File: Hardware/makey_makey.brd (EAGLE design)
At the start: 94 x 48.3 mm, 73 parts, among them U1 ATMEGA32U4TQFP, X1 USBSMD, Y1 16MHz

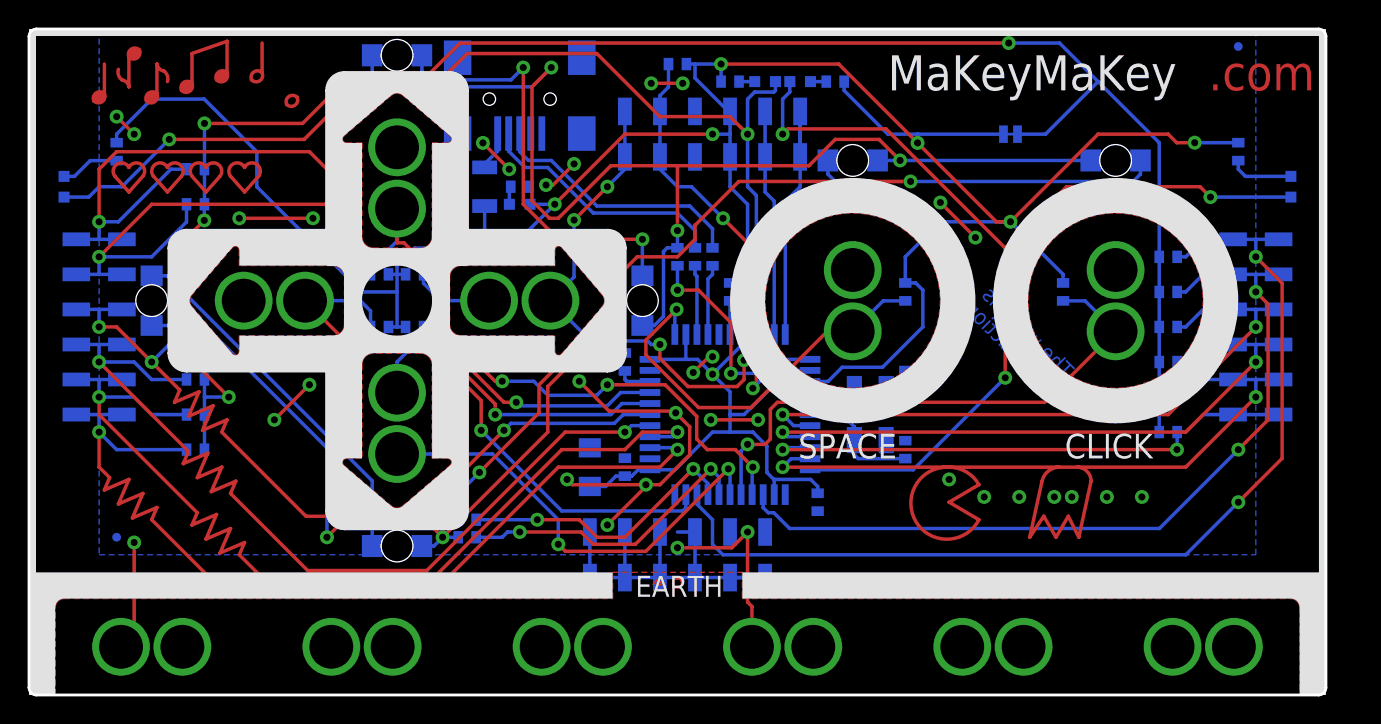
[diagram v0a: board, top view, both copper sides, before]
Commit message: QC Revision
1.) Switch 0402 to 0603 footprints
2.) Updated to wide PTC footprint
3.) Added more bstop over lead banks on 32u4 IC for better AOI.
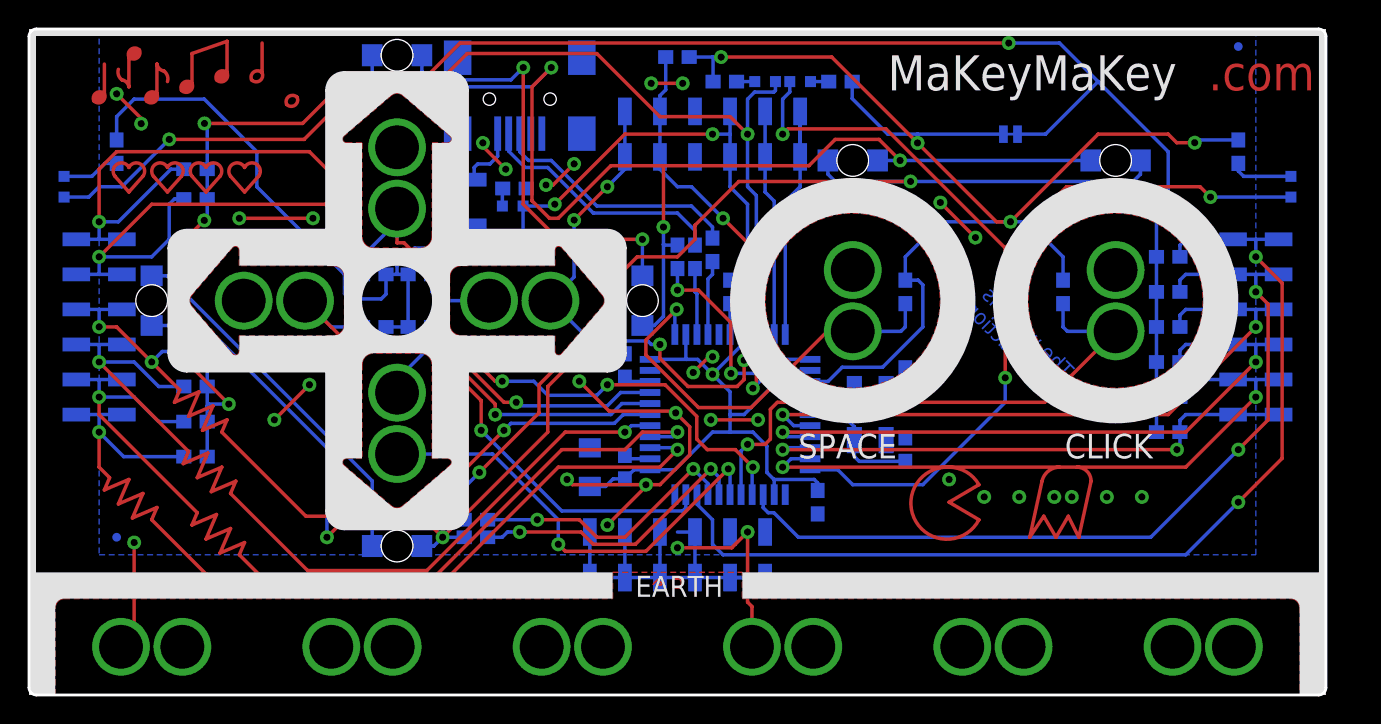
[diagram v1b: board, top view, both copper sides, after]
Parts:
- C1, C2, C3, C4, C5, C6, C8: device SparkFun:0402-CAP -> SparkFun:0603-CAP
- F1: device SparkFun-PowerIC:PTC-1206 -> SparkFun-PowerIC:PTC-1206-WIDE
- R1, R10, R11, R12, R13, R14, R15, R2, R23, R24, R25, R26, R27, R28, R29, R3, R4, R5, R6, R7, R8, R9: device SparkFun:0402-RES -> SparkFun:0603-RES
- R16, R17, R18, R19, R20, R21, R22: device SparkFun-Passives:0402-RES -> SparkFun-Passives:0603-RES
- moved F1 1.37 mm to (32.3, 35.7)
- moved C8 0.85 mm to (30.1, 36.1)
- moved R20 0.63 mm to (32.4, 11.4)
- moved R21 0.63 mm to (32.4, 12.7)
- moved LED7 0.52 mm to (35.1, 35.4)
- moved R2 0.51 mm to (49.5, 32.3)
- moved R3 0.51 mm to (47.0, 46.2)
- moved R4 0.51 mm to (12.1, 17.3)
- moved R5 0.51 mm to (12.1, 19.8)
- moved R6 0.51 mm to (12.1, 22.4)
- moved R7 0.51 mm to (12.1, 24.9)
- moved R23 0.40 mm to (35.2, 36.7)
- moved R16 0.38 mm to (58.8, 44.5)
- moved R19 0.38 mm to (50.4, 44.5)
- moved R24 0.38 mm to (25.0, 30.5)
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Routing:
- net VCC: track 233.0 -> 229.7 mm
- net GND: track 104.3 -> 107.2 mm
- net PD5: track 73.0 -> 75.0 mm
- net N$5: track 2.84 -> 4.56 mm
- net D13: track 42.4 -> 41.2 mm
- net PULL-UP: track 134.5 -> 135.7 mm
- net D7: track 29.7 -> 30.6 mm
- net D6: track 39.9 -> 40.8 mm
- net D9: track 21.9 -> 21.1 mm
- net D10: track 20.6 -> 19.8 mm
- net D4: track 60.2 -> 61.0 mm
- net A4: track 66.0 -> 66.7 mm
- net N$8: track 19.0 -> 18.3 mm

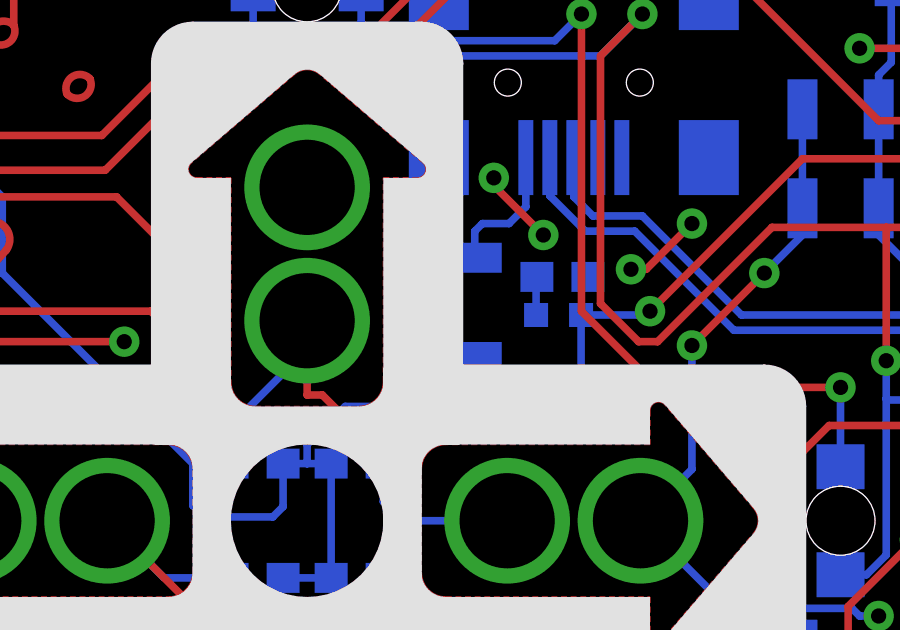
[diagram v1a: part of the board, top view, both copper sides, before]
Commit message: Swapped positions of PTC and C8
Swapped the positions of PTC and C8 to better accommodate and center the
"POWER" silk.
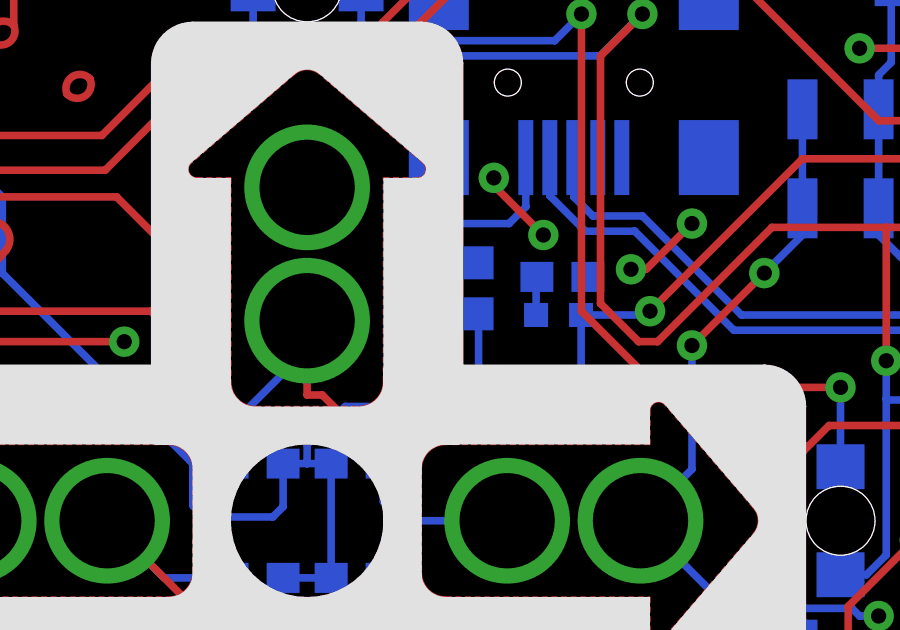
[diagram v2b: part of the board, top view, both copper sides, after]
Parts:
- moved C8 2.30 mm to (32.4, 36.3)
- moved F1 1.78 mm to (30.5, 35.6)
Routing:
- net N$5: track 4.56 -> 6.40 mm
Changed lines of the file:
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@@
 <vertex x="22.86" y="26.035"/>
 </polygon>
-<text x="35.433" y="34.417" size="1.143" layer="22" ratio="18" rot="MR0" align="top-center">POWER</text>
+<text x="34.925" y="34.29" size="1.143" layer="22" ratio="18" rot="MR0" align="top-center">POWER</text>
 <text x="78.74" y="33.909" size="1.524" layer="22" ratio="18" rot="MR0" align="center">CLICK</text>
 <text x="59.69" y="33.909" size="1.524" layer="22" ratio="18" rot="MR0" align="center">SPACE</text>
@@
 <element name="R23" library="SparkFun" package="0603-RES" value="1k" x="35.179" y="36.703" rot="MR0"/>
 <element name="LED7" library="SparkFun" package="LED-0603" value="RED" x="35.052" y="35.433" rot="MR270"/>
-<element name="C8" library="SparkFun" package="0603-CAP" value="0.1uF" x="30.099" y="36.068" rot="MR270"/>
+<element name="C8" library="SparkFun" package="0603-CAP" value="0.1uF" x="32.385" y="36.322" rot="MR270"/>
 <element name="R14" library="SparkFun" package="0603-RES" value="22M" x="82.55" y="29.21" rot="MR0"/>
 <element name="R13" library="SparkFun" package="0603-RES" value="22M" x="82.55" y="26.67" rot="MR0"/>
@@
 <element name="R21" library="SparkFun-Passives" package="0603-RES" value="330" x="32.385" y="12.7" rot="MR0"/>
 <element name="R22" library="SparkFun-Passives" package="0603-RES" value="330" x="46.99" y="31.75" rot="MR90"/>
-<element name="F1" library="SparkFun-PowerIC" package="PTC-1206-WIDE" value="500mA" x="32.258" y="35.687" rot="MR270"/>
+<element name="F1" library="SparkFun-PowerIC" package="PTC-1206-WIDE" value="500mA" x="30.48" y="35.56" rot="MR270"/>
 <element name="U$1" library="SparkFun-Aesthetics" package="OSHW-LOGO-M" value="OSHW-LOGOM" x="83.312" y="45.212" rot="MR0"/>
 <element name="SJ1" library="SparkFun" package="SJ_2S-TRACE" value="Pull-ups" x="71.12" y="40.64" rot="MR180"/>
@@
 <via x="38.1" y="35.56" extent="1-16" drill="0.508"/>
 <wire x1="51.6" y1="26.12" x2="51.6" y2="25.311" width="0.254" layer="16"/>
-<wire x1="27.94" y1="32.385" x2="30.099" y2="32.385" width="0.254" layer="16"/>
 <contactref element="SJ1" pad="1"/>
-<wire x1="30.099" y1="32.385" x2="32.258" y2="32.385" width="0.254" layer="16"/>
-<wire x1="32.258" y1="32.385" x2="34.925" y2="32.385" width="0.254" layer="16"/>
+<wire x1="27.94" y1="32.385" x2="30.48" y2="32.385" width="0.254" layer="16"/>
 <contactref element="LED7" pad="A"/>
+<wire x1="30.48" y1="32.385" x2="32.385" y2="32.385" width="0.254" layer="16"/>
+<wire x1="32.385" y1="32.385" x2="34.925" y2="32.385" width="0.254" layer="16"/>
 <wire x1="57.15" y1="14.82" x2="57.15" y2="15.367" width="0.254" layer="16"/>
 <wire x1="56.896" y1="15.621" x2="54" y2="15.621" width="0.254" layer="16"/>
@@
 <wire x1="59.651" y1="44.45" x2="59.651" y2="43.219" width="0.254" layer="16"/>
 <wire x1="59.651" y1="43.219" x2="62.23" y2="40.64" width="0.254" layer="16"/>
-<wire x1="30.099" y1="35.218" x2="30.099" y2="32.385" width="0.254" layer="16"/>
-<wire x1="32.258" y1="34.033" x2="32.258" y2="32.385" width="0.254" layer="16"/>
 <wire x1="35.802" y1="35.433" x2="35.802" y2="33.262" width="0.254" layer="16"/>
 <wire x1="35.802" y1="33.262" x2="34.925" y2="32.385" width="0.254" layer="16"/>
@@
 <wire x1="7.62" y1="43.18" x2="6.35" y2="41.91" width="0.254" layer="16"/>
 <wire x1="6.35" y1="41.91" x2="6.35" y2="40.22" width="0.254" layer="16"/>
+<wire x1="30.48" y1="33.906" x2="30.48" y2="32.385" width="0.254" layer="16"/>
+<wire x1="32.385" y1="35.472" x2="32.385" y2="32.385" width="0.254" layer="16"/>
 </signal>
 <signal name="N$1">
@@
 <wire x1="33.96" y1="40.68" x2="33.96" y2="39.04" width="0.254" layer="16"/>
 <wire x1="33.96" y1="39.04" x2="33.401" y2="38.481" width="0.254" layer="16"/>
-<wire x1="32.258" y1="37.341" x2="32.258" y2="38.227" width="0.254" layer="16"/>
-<wire x1="32.258" y1="38.227" x2="32.512" y2="38.481" width="0.254" layer="16"/>
-<wire x1="32.512" y1="38.481" x2="33.401" y2="38.481" width="0.254" layer="16"/>
+<wire x1="30.48" y1="37.214" x2="30.48" y2="38.1" width="0.254" layer="16"/>
+<wire x1="33.401" y1="38.481" x2="30.861" y2="38.481" width="0.254" layer="16"/>
+<wire x1="30.861" y1="38.481" x2="30.48" y2="38.1" width="0.254" layer="16"/>
 </signal>
 <signal name="N$7">
